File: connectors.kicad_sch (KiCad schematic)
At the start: 9 parts, among them J1 USB_C_Receptacle_USB2.0, J2 Motor_1_input, J3 Motor_2_input, J4 Power_Input, J5 Screw_Terminal_01x02, U3 USBLC6-2SC6

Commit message: Update placement
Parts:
- removed J5: Screw_Terminal_01x02, TerminalBlock:TerminalBlock_bornier-2_P5.08mm, symbol Connector:Screw_Terminal_01x02
- added J3: MOTOR_4_OUTPUT, TerminalBlock:TerminalBlock_bornier-2_P5.08mm, symbol Connector:Screw_Terminal_01x02
- added J3: MOTOR_3_OUTPUT, TerminalBlock:TerminalBlock_bornier-2_P5.08mm, symbol Connector:Screw_Terminal_01x02
- J2: value Motor_1_input -> MOTOR_1_OUTPUT
- J3: value Motor_2_input -> MOTOR_2_OUTPUT
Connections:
- net MOTOR_1_OUT_1: now also J2.1 (Pin_1); no longer J2.2 (Pin_2)
- net MOTOR_1_OUT_2: now also J2.2 (Pin_2); no longer J2.1 (Pin_1)
- net MOTOR_2_OUT_1: now also J3.1 (Pin_1); no longer J3.2 (Pin_2)
- net MOTOR_2_OUT_2: now also J3.2 (Pin_2); no longer J3.1 (Pin_1)
- new net MOTOR_3_OUT_1: J3.1 (Pin_1)
- new net MOTOR_3_OUT_2: J3.2 (Pin_2)
- new net MOTOR_4_OUT_1: J3.1 (Pin_1)
- new net MOTOR_4_OUT_2: J3.2 (Pin_2)
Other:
- moved on the sheet: J2, J3, J4

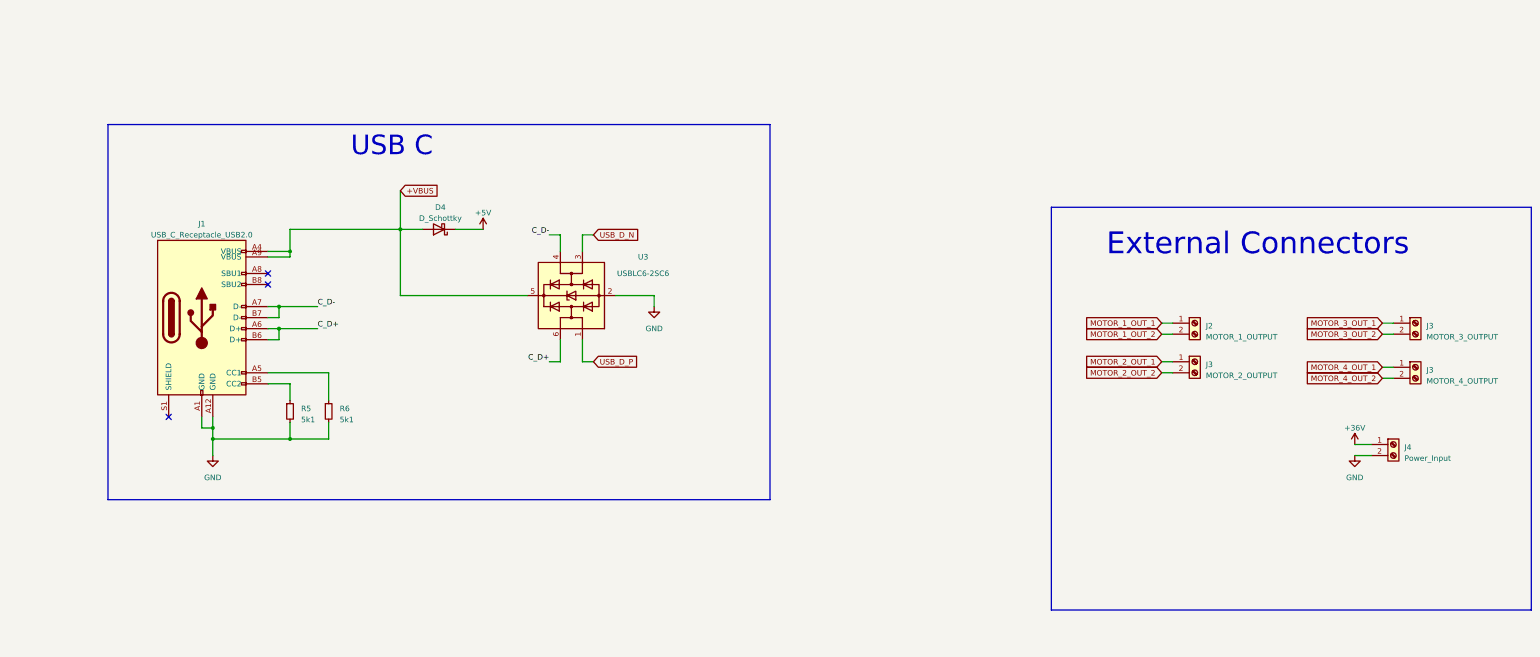
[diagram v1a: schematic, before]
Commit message: route usb and flash
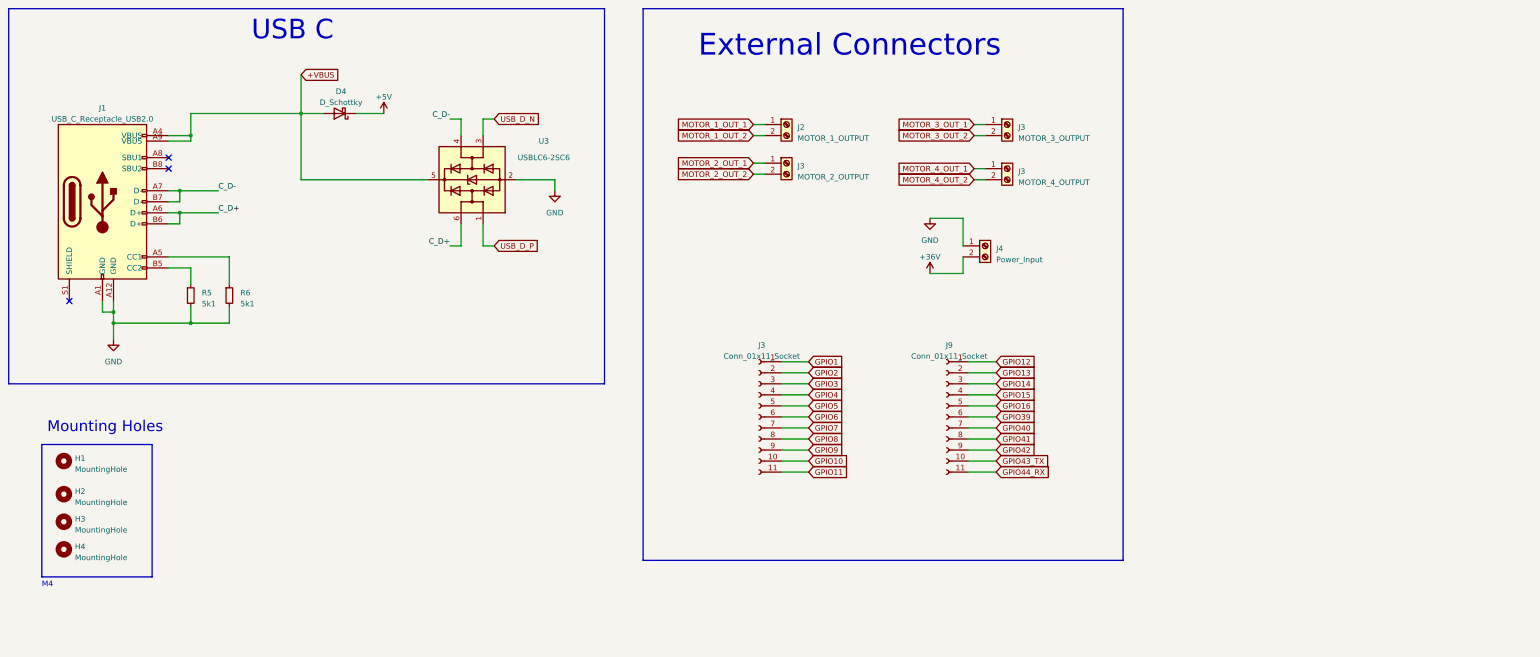
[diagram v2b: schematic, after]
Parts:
- added H1, H2, H3, H4: MountingHole, MountingHole:MountingHole_4.3mm_M4, symbol Mechanical:MountingHole
- added J3, J9: Conn_01x11_Socket, Connector_PinHeader_2.54mm:PinHeader_1x11_P2.54mm_Vertical_SMD_Pin1Left, symbol Connector:Conn_01x11_Socket
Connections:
- net +36V: now also J4.2 (Pin_2); no longer J4.1 (Pin_1)
- net GND: now also J4.1 (Pin_1); no longer J4.2 (Pin_2)
- new net GPIO1: J3.1 (Pin_1)
- new net GPIO10: J3.10 (Pin_10)
- new net GPIO11: J3.11 (Pin_11)
- new net GPIO12: J9.1 (Pin_1)
- new net GPIO13: J9.2 (Pin_2)
- new net GPIO14: J9.3 (Pin_3)
- new net GPIO15: J9.4 (Pin_4)
- new net GPIO16: J9.5 (Pin_5)
- new net GPIO2: J3.2 (Pin_2)
- new net GPIO3: J3.3 (Pin_3)
- new net GPIO39: J9.6 (Pin_6)
- new net GPIO4: J3.4 (Pin_4)
- new net GPIO40: J9.7 (Pin_7)
- new net GPIO41: J9.8 (Pin_8)
- new net GPIO42: J9.9 (Pin_9)
- new net GPIO43_TX: J9.10 (Pin_10)
- new net GPIO44_RX: J9.11 (Pin_11)
- new net GPIO5: J3.5 (Pin_5)
- new net GPIO6: J3.6 (Pin_6)
- new net GPIO7: J3.7 (Pin_7)
- new net GPIO8: J3.8 (Pin_8)
- new net GPIO9: J3.9 (Pin_9)
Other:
- note added: "M4"
- note added: "Mounting Holes"
- moved on the sheet: D4, J1, J2, J3, J4, R5, R6, U3

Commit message: route motors
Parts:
- added J8: Conn_01x03_Socket, Connector_PinSocket_2.54mm:PinSocket_1x03_P2.54mm_Vertical, symbol Connector:Conn_01x03_Socket
- renumbered J4 to J2, J2 to J4, J3 to J5, J3 to J6, J3 to J7, R5 to R2, R6 to R3
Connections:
- net +5V: now also J8.2 (Pin_2)
- net GND: now also J8.3 (Pin_3)
- new net +3V3: J8.1 (Pin_1)

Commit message: checkpoint for backup
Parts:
- added JP1: Jumper_PMODE, Connector_PinHeader_2.54mm:PinHeader_1x03_P2.54mm_Vertical_SMD_Pin1Right, symbol Jumper:Jumper_3_Bridged12
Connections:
- net +36V: now also J2.1 (Pin_1); no longer J2.2 (Pin_2)
- net +3V3: now also JP1.1 (A)
- net GND: now also J2.2 (Pin_2), JP1.3 (B); no longer J2.1 (Pin_1)
- net GPIO10: no longer names the net of J3.10 (Pin_10)
- net GPIO11: no longer names the net of J3.11 (Pin_11)
- net GPIO12: no longer names the net of J9.1 (Pin_1)
- net GPIO13: no longer names the net of J9.2 (Pin_2)
- net GPIO15 renamed GPIO17
- net GPIO16 renamed GPIO18
- net GPIO7: no longer names the net of J3.7 (Pin_7)
- net GPIO8: no longer names the net of J3.8 (Pin_8)
- net GPIO9: no longer names the net of J3.9 (Pin_9)
- new net MOTOR_PMODE: JP1.2 (C)
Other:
- moved on the sheet: J2

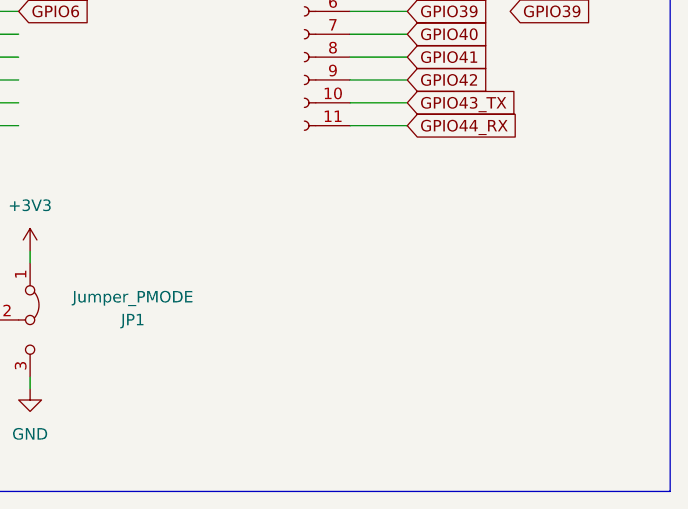
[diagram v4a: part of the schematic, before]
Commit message: Replace MCU with WROOM-1 unit + route
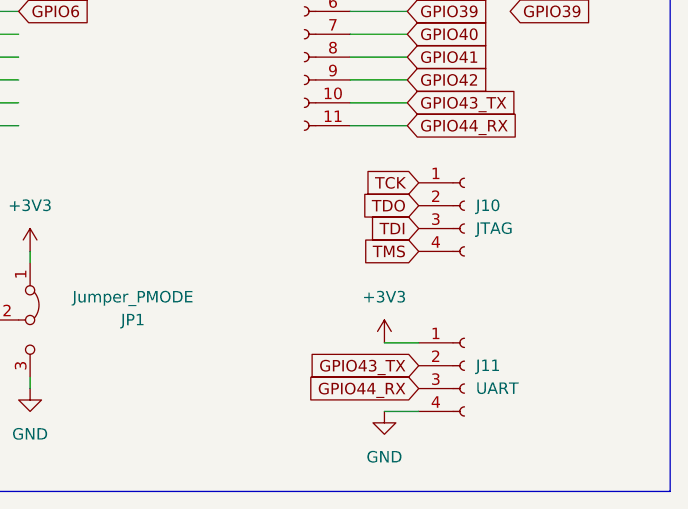
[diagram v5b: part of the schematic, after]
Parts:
- added J10: JTAG, Connector_PinHeader_2.54mm:PinHeader_1x04_P2.54mm_Vertical_SMD_Pin1Right, symbol Connector:Conn_01x04_Socket
- added J11: UART, Connector_PinHeader_2.54mm:PinHeader_1x04_P2.54mm_Vertical_SMD_Pin1Right, symbol Connector:Conn_01x04_Socket
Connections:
- net +3V3: now also J11.1 (Pin_1)
- net GND: now also J11.4 (Pin_4)
- net GPIO43_TX: now also J11.2 (Pin_2)
- net GPIO44_RX: now also J11.3 (Pin_3)
- new net TCK: J10.1 (Pin_1)
- new net TDI: J10.3 (Pin_3)
- new net TDO: J10.2 (Pin_2)
- new net TMS: J10.4 (Pin_4)
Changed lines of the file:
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@@
+    (stroke (width 0) (type default))
+  )
+  (wire (pts (xy 242.57 154.94) (xy 246.38 154.94))
     (stroke (width 0) (type default))
   )
@@
   )
   (wire (pts (xy 114.3 55.88) (xy 85.09 55.88))
+    (stroke (width 0) (type default))
+  )
+  (wire (pts (xy 242.57 147.32) (xy 246.38 147.32))
     (stroke (width 0) (type default))
   )
@@
     )
   )
+  (global_label "TDO" (shape input) (at 246.38 132.08 180) (fields_autoplaced)
+    (effects (font (size 1.27 1.27)) (justify right))
+    (property "Intersheetrefs" "${INTERSHEET_REFS}" (at 239.8267 132.08 0)
+      (effects (font (size 1.27 1.27)) (justify right) hide)
+    )
+  )
   (global_label "USB_D_N" (shape input) (at 129.54 41.91 0) (fields_autoplaced)
     (effects (font (size 1.27 1.27)) (justify left))
@@
     )
   )
+  (global_label "GPIO43_TX" (shape input) (at 246.38 149.86 180) (fields_autoplaced)
+    (effects (font (size 1.27 1.27)) (justify right))
+    (property "Intersheetrefs" "${INTERSHEET_REFS}" (at 233.3558 149.86 0)
+      (effects (font (size 1.27 1.27)) (justify right) hide)
+    )
+  )
   (global_label "MOTOR_4_OUT_2" (shape input) (at 240.03 55.88 180) (fields_autoplaced)
     (effects (font (size 1.27 1.27)) (justify right))
@@
     )
   )
+  (global_label "TMS" (shape input) (at 246.38 137.16 180) (fields_autoplaced)
+    (effects (font (size 1.27 1.27)) (justify right))
+    (property "Intersheetrefs" "${INTERSHEET_REFS}" (at 239.7663 137.16 0)
+      (effects (font (size 1.27 1.27)) (justify right) hide)
+    )
+  )
+  (global_label "TCK" (shape input) (at 246.38 129.54 180) (fields_autoplaced)
+    (effects (font (size 1.27 1.27)) (justify right))
+    (property "Intersheetrefs" "${INTERSHEET_REFS}" (at 239.8872 129.54 0)
+      (effects (font (size 1.27 1.27)) (justify right) hide)
+    )
+  )
   (global_label "GPIO18" (shape input) (at 245.11 107.95 0) (fields_autoplaced)
     (effects (font (size 1.27 1.27)) (justify left))
@@
     )
   )
+  (global_label "GPIO44_RX" (shape input) (at 246.38 152.4 180) (fields_autoplaced)
+    (effects (font (size 1.27 1.27)) (justify right))
+    (property "Intersheetrefs" "${INTERSHEET_REFS}" (at 233.0534 152.4 0)
+      (effects (font (size 1.27 1.27)) (justify right) hide)
+    )
+  )
   (global_label "USB_D_P" (shape input) (at 129.54 71.12 0) (fields_autoplaced)
     (effects (font (size 1.27 1.27)) (justify left))
@@
     (effects (font (size 1.27 1.27)) (justify right))
     (property "Intersheetrefs" "${INTERSHEET_REFS}" (at 171.0238 54.61 0)
+      (effects (font (size 1.27 1.27)) (justify right) hide)
+    )
+  )
+  (global_label "TDI" (shape input) (at 246.38 134.62 180) (fields_autoplaced)
+    (effects (font (size 1.27 1.27)) (justify right))
+    (property "Intersheetrefs" "${INTERSHEET_REFS}" (at 240.5524 134.62 0)
       (effects (font (size 1.27 1.27)) (justify right) hide)
     )
@@
         (path "/6532ed18-dd14-44a4-a4f8-6383f8135b66/4e5677ed-0dc8-49f6-a11b-e4c4e0cc396f"
           (reference "#PWR012") (unit 1)
+        )
+      )
+    )
+  )
+  (symbol (lib_id "Connector:Conn_01x04_Socket") (at 251.46 149.86 0) (unit 1)
+    (in_bom yes) (on_board yes) (dnp no) (fields_autoplaced)
+    (property "Reference" "J11" (at 252.73 149.86 0)
+      (effects (font (size 1.27 1.27)) (justify left))
+    )
+    (property "Value" "UART" (at 252.73 152.4 0)
+      (effects (font (size 1.27 1.27)) (justify left))
+    )
+    (property "Footprint" "Connector_PinHeader_2.54mm:PinHeader_1x04_P2.54mm_Vertical_SMD_Pin1Right" (at 251.46 149.86 0)
+      (effects (font (size 1.27 1.27)) hide)
+    )
+    (property "Datasheet" "~" (at 251.46 149.86 0)
+      (effects (font (size 1.27 1.27)) hide)
+    )
+    (pin "1")
+    (pin "3")
+    (pin "2")
+    (pin "4")
+    (instances
+      (project "RC-Car-Controller"
+        (path "/6532ed18-dd14-44a4-a4f8-6383f8135b66/4e5677ed-0dc8-49f6-a11b-e4c4e0cc396f"
+          (reference "J11") (unit 1)
         )
       )
@@
     )
   )
+  (symbol (lib_id "power:GND") (at 242.57 154.94 0) (unit 1)
+    (in_bom yes) (on_board yes) (dnp no) (fields_autoplaced)
+    (property "Reference" "#PWR031" (at 242.57 161.29 0)
+      (effects (font (size 1.27 1.27)) hide)
+    )
+    (property "Value" "GND" (at 242.57 160.02 0)
+      (effects (font (size 1.27 1.27)))
+    )
+    (property "Footprint" "" (at 242.57 154.94 0)
+      (effects (font (size 1.27 1.27)) hide)
+    )
+    (property "Datasheet" "" (at 242.57 154.94 0)
+      (effects (font (size 1.27 1.27)) hide)
+    )
+    (pin "1")
+    (instances
+      (project "RC-Car-Controller"
+        (path "/6532ed18-dd14-44a4-a4f8-6383f8135b66/4e5677ed-0dc8-49f6-a11b-e4c4e0cc396f"
+          (reference "#PWR031") (unit 1)
+        )
+      )
+    )
+  )
   (symbol (lib_id "Mechanical:MountingHole") (at 30.48 134.62 0) (unit 1)
     (in_bom yes) (on_board yes) (dnp no) (fields_autoplaced)
@@
         )
       )
+    )
+  )
+  (symbol (lib_id "Connector:Conn_01x04_Socket") (at 251.46 132.08 0) (unit 1)
+    (in_bom yes) (on_board yes) (dnp no) (fields_autoplaced)
+    (property "Reference" "J10" (at 252.73 132.08 0)
+      (effects (font (size 1.27 1.27)) (justify left))
+    )
+    (property "Value" "JTAG" (at 252.73 134.62 0)
+      (effects (font (size 1.27 1.27)) (justify left))
+    )
+    (property "Footprint" "Connector_PinHeader_2.54mm:PinHeader_1x04_P2.54mm_Vertical_SMD_Pin1Right" (at 251.46 132.08 0)
+      (effects (font (size 1.27 1.27)) hide)
+    )
+    (property "Datasheet" "~" (at 251.46 132.08 0)
+      (effects (font (size 1.27 1.27)) hide)
+    )
+    (pin "1")
+    (pin "3")
+    (pin "2")
+    (pin "4")
+    (instances
+      (project "RC-Car-Controller"
+        (path "/6532ed18-dd14-44a4-a4f8-6383f8135b66/4e5677ed-0dc8-49f6-a11b-e4c4e0cc396f"
+          (reference "J10") (unit 1)
+        )
+      )
+    )
+  )
+  (symbol (lib_id "power:+3V3") (at 242.57 147.32 0) (unit 1)
+    (in_bom yes) (on_board yes) (dnp no) (fields_autoplaced)
+    (property "Reference" "#PWR030" (at 242.57 151.13 0)
+      (effects (font (size 1.27 1.27)) hide)
+    )
+    (property "Value" "+3V3" (at 242.57 142.24 0)
+      (effects (font (size 1.27 1.27)))
+    )
+    (property "Footprint" "" (at 242.57 147.32 0)
+      (effects (font (size 1.27 1.27)) hide)
+    )
+    (property "Datasheet" "" (at 242.57 147.32 0)
+      (effects (font (size 1.27 1.27)) hide)
+    )
+    (pin "1")
+    (instances
+      (project "RC-Car-Controller"
+        (path "/6532ed18-dd14-44a4-a4f8-6383f8135b66/4e5677ed-0dc8-49f6-a11b-e4c4e0cc396f"
+          (reference "#PWR030") (unit 1)
+        )
+      )

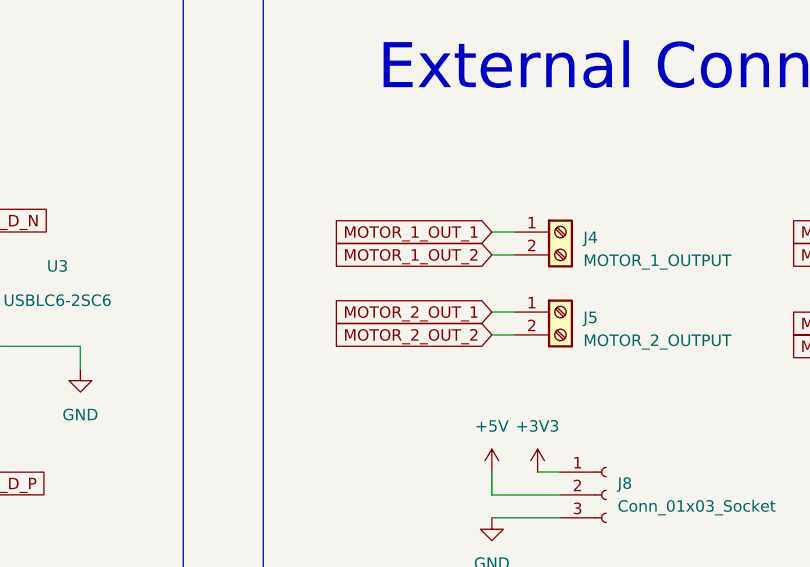
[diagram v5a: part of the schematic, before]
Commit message: Route Motor Drivers
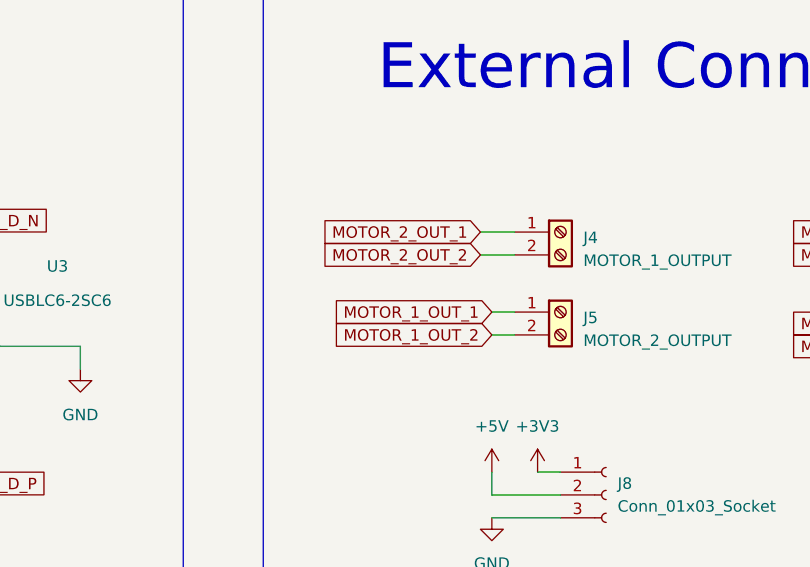
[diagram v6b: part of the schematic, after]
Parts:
- J9: footprint Connector_PinHeader_2.54mm:PinHeader_1x11_P2.54mm_Vertical_SMD_Pin1Left -> Connector_PinHeader_2.54mm:PinHeader_1x11_P2.54mm_Vertical
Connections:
- net MOTOR_1_OUT_1: now also J5.1 (Pin_1); no longer J4.1 (Pin_1)
- net MOTOR_1_OUT_2: now also J5.2 (Pin_2); no longer J4.2 (Pin_2)
- net MOTOR_2_OUT_1: now also J4.1 (Pin_1); no longer J5.1 (Pin_1)
- net MOTOR_2_OUT_2: now also J4.2 (Pin_2); no longer J5.2 (Pin_2)
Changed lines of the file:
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@@
+    (stroke (width 0) (type default))
+  )
+  (wire (pts (xy 189.23 54.61) (xy 191.77 54.61))
     (stroke (width 0) (type default))
   )
@@
     (stroke (width 0) (type default))
   )
-  (wire (pts (xy 189.23 43.18) (xy 191.77 43.18))
+  (wire (pts (xy 187.96 43.18) (xy 191.77 43.18))
     (stroke (width 0) (type default))
   )
@@
     (stroke (width 0) (type default))
   )
-  (wire (pts (xy 189.23 54.61) (xy 191.77 54.61))
-    (stroke (width 0) (type default))
-  )
   (wire (pts (xy 189.23 74.93) (xy 196.85 74.93))
     (stroke (width 0) (type default))
@@
     (stroke (width 0) (type default))
   )
+  (wire (pts (xy 189.23 52.07) (xy 191.77 52.07))
+    (stroke (width 0) (type default))
+  )
   (wire (pts (xy 195.58 115.57) (xy 201.93 115.57))
     (stroke (width 0) (type default))
@@
     (stroke (width 0) (type default))
   )
-  (wire (pts (xy 189.23 52.07) (xy 191.77 52.07))
-    (stroke (width 0) (type default))
-  )
   (wire (pts (xy 127 41.91) (xy 127 45.72))
     (stroke (width 0) (type default))
@@
     (stroke (width 0) (type default))
   )
+  (wire (pts (xy 187.96 45.72) (xy 191.77 45.72))
+    (stroke (width 0) (type default))
+  )
   (wire (pts (xy 143.51 58.42) (xy 143.51 55.88))
     (stroke (width 0) (type default))
@@
   )
   (wire (pts (xy 54.61 58.42) (xy 57.15 58.42))
-    (stroke (width 0) (type default))
-  )
-  (wire (pts (xy 189.23 45.72) (xy 191.77 45.72))
     (stroke (width 0) (type default))
   )
@@
     )
   )
-  (global_label "MOTOR_1_OUT_2" (shape input) (at 189.23 45.72 180) (fields_autoplaced)
-    (effects (font (size 1.27 1.27)) (justify right))
-    (property "Intersheetrefs" "${INTERSHEET_REFS}" (at 171.0238 45.72 0)
-      (effects (font (size 1.27 1.27)) (justify right) hide)
-    )
-  )
-  (global_label "MOTOR_1_OUT_1" (shape input) (at 189.23 43.18 180) (fields_autoplaced)
-    (effects (font (size 1.27 1.27)) (justify right))
-    (property "Intersheetrefs" "${INTERSHEET_REFS}" (at 171.0238 43.18 0)
+  (global_label "MOTOR_1_OUT_2" (shape input) (at 189.23 54.61 180) (fields_autoplaced)
+    (effects (font (size 1.27 1.27)) (justify right))
+    (property "Intersheetrefs" "${INTERSHEET_REFS}" (at 171.0238 54.61 0)
+      (effects (font (size 1.27 1.27)) (justify right) hide)
+    )
+  )
+  (global_label "MOTOR_1_OUT_1" (shape input) (at 189.23 52.07 180) (fields_autoplaced)
+    (effects (font (size 1.27 1.27)) (justify right))
+    (property "Intersheetrefs" "${INTERSHEET_REFS}" (at 171.0238 52.07 0)
       (effects (font (size 1.27 1.27)) (justify right) hide)
     )
@@
     )
   )
-  (global_label "MOTOR_2_OUT_1" (shape input) (at 189.23 52.07 180) (fields_autoplaced)
-    (effects (font (size 1.27 1.27)) (justify right))
-    (property "Intersheetrefs" "${INTERSHEET_REFS}" (at 171.0238 52.07 0)
+  (global_label "MOTOR_2_OUT_1" (shape input) (at 187.96 43.18 180) (fields_autoplaced)
+    (effects (font (size 1.27 1.27)) (justify right))
+    (property "Intersheetrefs" "${INTERSHEET_REFS}" (at 169.7538 43.18 0)
       (effects (font (size 1.27 1.27)) (justify right) hide)
     )
@@
     )
   )
-  (global_label "MOTOR_2_OUT_2" (shape input) (at 189.23 54.61 180) (fields_autoplaced)
-    (effects (font (size 1.27 1.27)) (justify right))
-    (property "Intersheetrefs" "${INTERSHEET_REFS}" (at 171.0238 54.61 0)
+  (global_label "MOTOR_2_OUT_2" (shape input) (at 187.96 45.72 180) (fields_autoplaced)
+    (effects (font (size 1.27 1.27)) (justify right))
+    (property "Intersheetrefs" "${INTERSHEET_REFS}" (at 169.7538 45.72 0)
       (effects (font (size 1.27 1.27)) (justify right) hide)
     )
@@
       (effects (font (size 1.27 1.27)))
     )
-    (property "Footprint" "Connector_PinHeader_2.54mm:PinHeader_1x11_P2.54mm_Vertical_SMD_Pin1Left" (at 233.68 110.49 0)
-      (effects (font (size 1.27 1.27)) hide)
-    )
+    (property "Footprint" "Connector_PinHeader_2.54mm:PinHeader_1x11_P2.54mm_Vertical" (at 233.68 110.49 0)
+      (effects (font (size 1.27 1.27)) hide)
+    )
